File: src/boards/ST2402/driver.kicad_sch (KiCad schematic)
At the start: 49 parts, among them J15 Screw_Terminal_01x01, J16 Screw_Terminal_01x01, J17 Screw_Terminal_01x01, J9 Screw_Terminal_01x02, Q1 STB100N10F7, Q2 STB100N10F7, U1 L6494LD

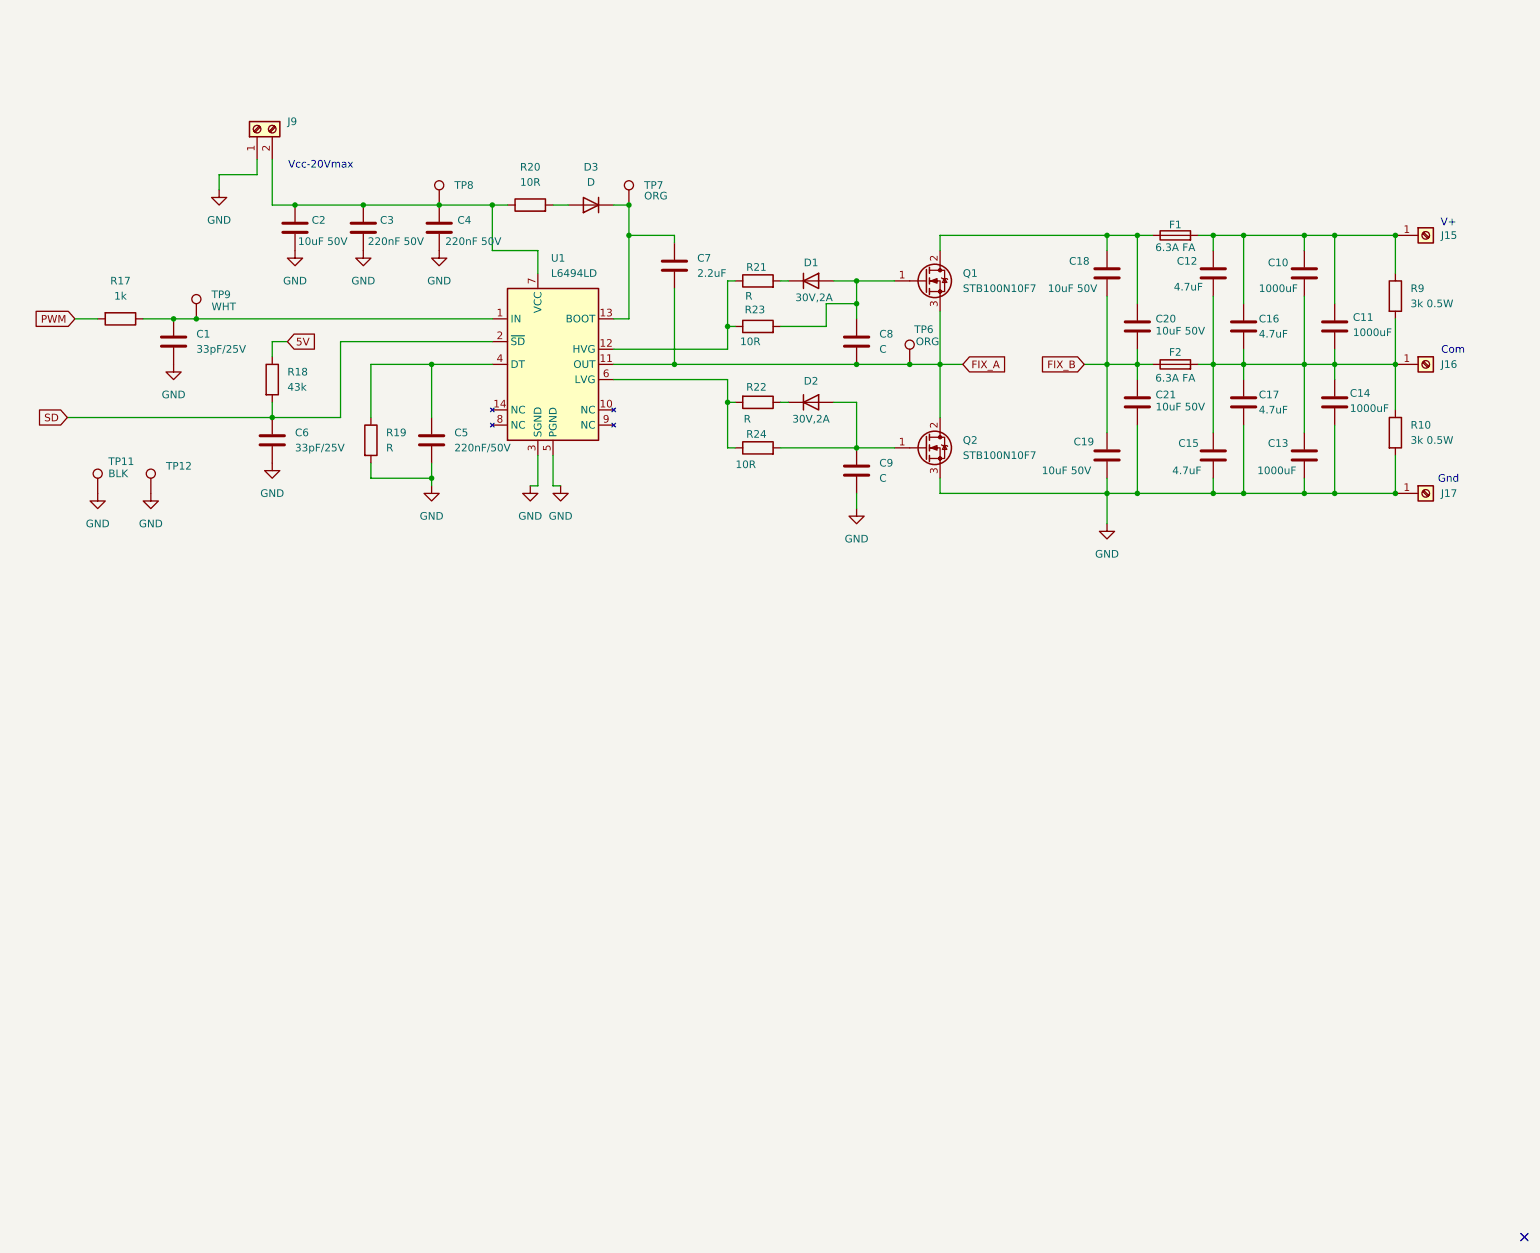
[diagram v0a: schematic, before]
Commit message: Updated pcb files
Added r2 and r3 gerbers and updated KiCad file (r3)
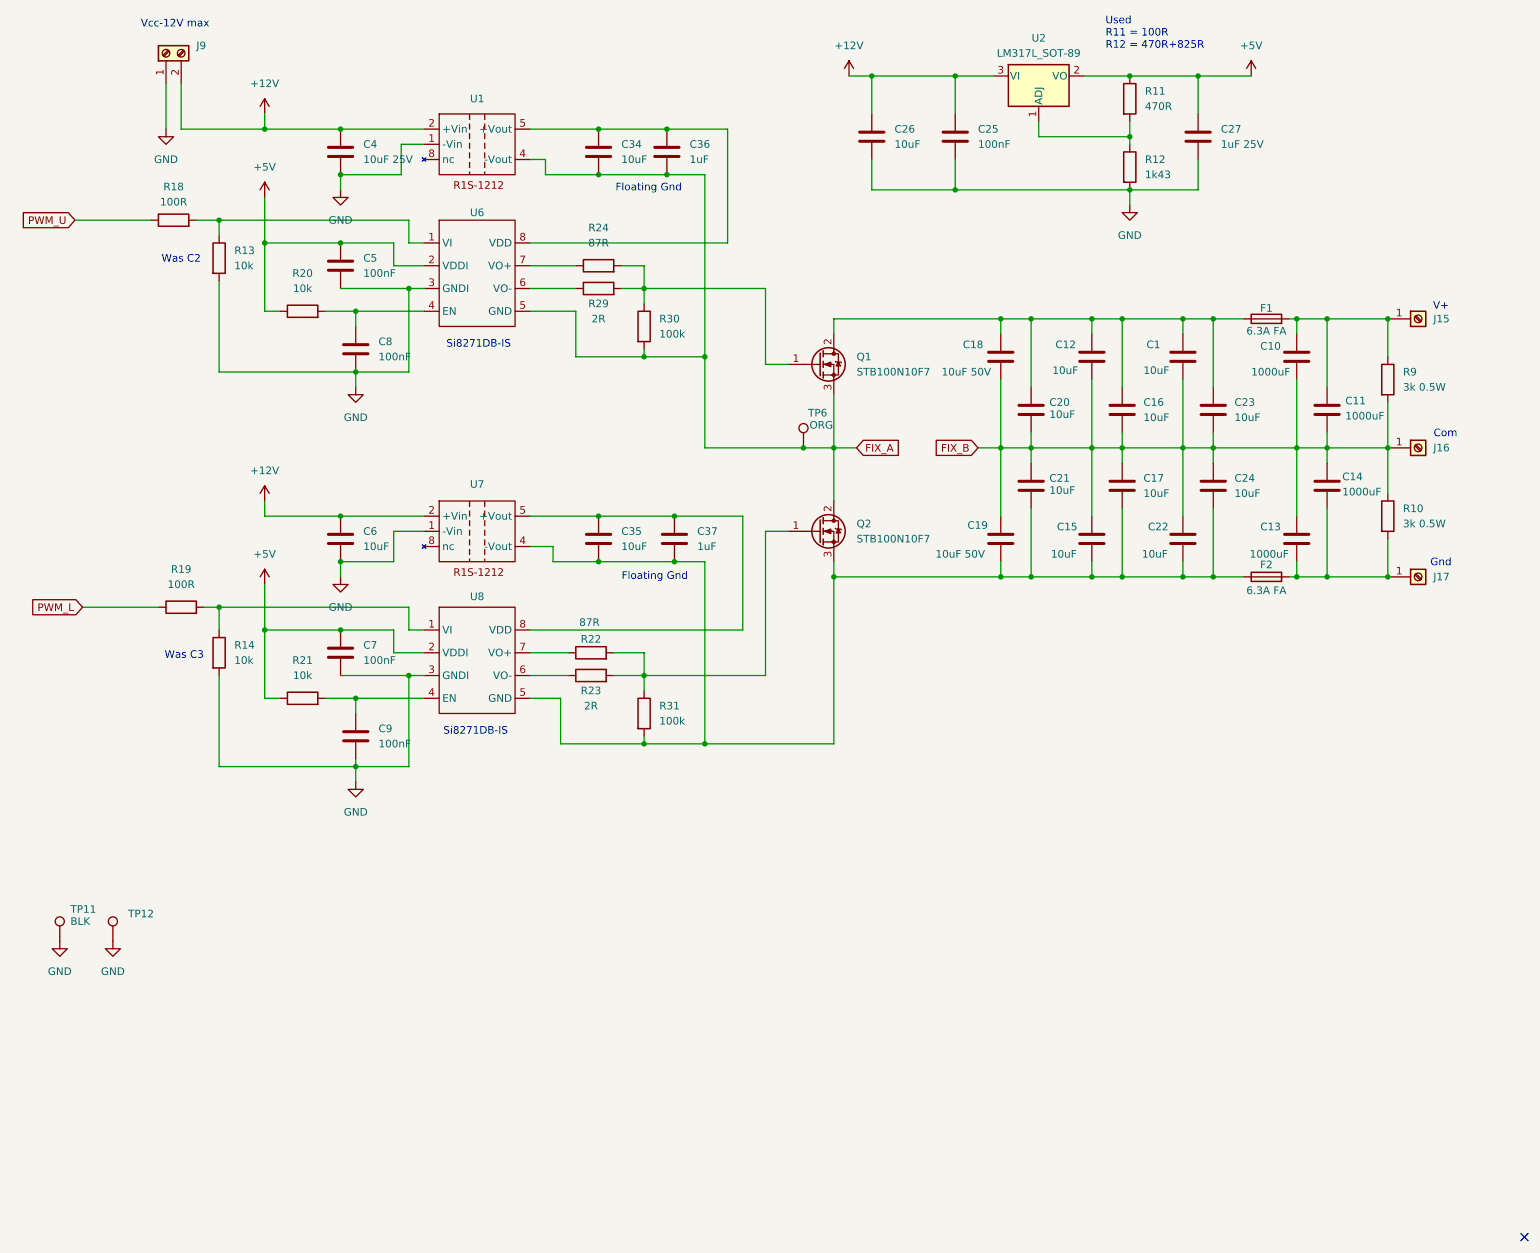
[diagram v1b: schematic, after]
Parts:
- removed C2: 10uF 50V, Capacitor_SMD:C_1206_3216Metric, symbol Device:C
- removed C3: 220nF 50V, Capacitor_SMD:C_0805_2012Metric, symbol Device:C
- removed D1, D2: 30V,2A, Diode_SMD:D_SMA, symbol Device:D
- removed D3: D, Diode_SMD:D_SMA, symbol Device:D
- removed R17: 1k, Resistor_SMD:R_0805_2012Metric, symbol Device:R
- removed TP7: ORG, TestPoint:TestPoint_THTPad_D2.0mm_Drill1.0mm, symbol Connector:TestPoint
- removed TP8: TestPoint, TestPoint:TestPoint_THTPad_D2.0mm_Drill1.0mm, symbol Connector:TestPoint
- removed TP9: WHT, TestPoint:TestPoint_THTPad_D2.0mm_Drill1.0mm, symbol Connector:TestPoint
- removed U1: L6494LD, Package_SO:SO-14_3.9x8.65mm_P1.27mm, symbol Driver_FET:L6491
- added C22, C23, C24: 10uF, Capacitor_SMD:C_1210_3225Metric, symbol Device:C
- added C25: 100nF, Capacitor_SMD:C_0805_2012Metric, symbol Device:C
- added C26, C34, C35: 10uF, Capacitor_SMD:C_0805_2012Metric, symbol Device:C
- added C27: 1uF 25V, Capacitor_SMD:C_0805_2012Metric, symbol Device:C
- added C36, C37: 1uF, Capacitor_SMD:C_0805_2012Metric, symbol Device:C
- added R11: 470R, Resistor_SMD:R_0805_2012Metric, symbol Device:R
- added R12: 1k43, Resistor_SMD:R_0805_2012Metric, symbol Device:R
- added R13, R14: 10k, Resistor_SMD:R_0805_2012Metric, symbol Device:R
- added R29: 2R, Resistor_SMD:R_0805_2012Metric, symbol Device:R
- added R30, R31: 100k, Resistor_SMD:R_0805_2012Metric, symbol Device:R
- added U1, U7: ~, GS_Library:5_pin_single_smd, symbol GS_Library:R1S-1212
- added U2: LM317L_SOT-89, Package_TO_SOT_SMD:SOT-89-3, symbol Regulator_Linear:LM317L_SOT-89
- added U6, U8: ~, Package_SO:SOIC-8_3.9x4.9mm_P1.27mm, symbol GS_Library:Si8271DB
- C1: value 33pF/25V -> 10uF; footprint Capacitor_SMD:C_0805_2012Metric -> Capacitor_SMD:C_1210_3225Metric
- C12, C15, C16, C17: value 4.7uF -> 10uF; footprint Capacitor_THT:C_Rect_L18.0mm_W11.0mm_P15.00mm_FKS3_FKP3 -> Capacitor_SMD:C_1210_3225Metric
- C20, C21: value 10uF 50V -> 10uF
- C4: value 220nF 50V -> 10uF 25V
- C5: value 220nF/50V -> 100nF
- C6: value 33pF/25V -> 10uF
- C7: value 2.2uF -> 100nF; footprint Capacitor_SMD:C_1206_3216Metric -> Capacitor_SMD:C_0805_2012Metric
- C8, C9: value C -> 100nF
- R18: value 43k -> 100R
- R19: value R -> 100R
- R20: value 10R -> 10k; footprint Resistor_SMD:R_1206_3216Metric -> Resistor_SMD:R_0805_2012Metric
- R21: value R -> 10k
- R22: value R -> 87R
- R23: value 10R -> 2R
- R24: value 10R -> 87R
- TP11, TP12, TP6: footprint TestPoint:TestPoint_THTPad_D2.0mm_Drill1.0mm -> TestPoint:TestPoint_Keystone_5010-5014_Multipurpose
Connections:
- net FIX_A: now also C34.2, C36.2, R30.2, U1.4 (-Vout), U6.5 (GND); no longer C7.2, C8.2
- net FIX_B: now also C1.2, C10.2, C11.2, C12.2, C13.1, C14.1, C15.1, C16.2, C17.1, J16.1 (Pin_1), R10.1, R9.2, C22.1, C23.2, C24.1; no longer F2.1
- net GND: now also C7.2, C8.2, C25.2, C26.2, C27.2, R12.2, R13.2, R14.2, U1.1 (-Vin), U6.3 (GNDI), U7.1 (-Vin), U8.3 (GNDI); no longer C1.2, C13.2, C14.2, C15.2, C17.2, C19.2, C21.2, J17.1 (Pin_1), Q2.3 (S), R10.2, R19.2
- net +12V: now reaches C4.1, J9.2 (Pin_2)
- net +12V: now also C6.1, C25.1, C26.1, U1.2 (+Vin), U2.3 (VI), U7.2 (+Vin); no longer R20.1
- net +5V: now reaches C5.1
- net +5V: now also C7.1, R20.1, R21.1, C27.1, R11.1, U2.2 (VO), U6.2 (VDDI), U8.2 (VDDI); no longer R19.1
- net at C10.1, C11.1, F1.2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: no longer C12.1, C16.1
- net at R23.1: now also U8.6 (VO-); no longer R21.1
- net at C1.1: now also C12.1, C16.1, C18.1, C20.1, F1.1, Q1.2 (D), C23.1
- net at R21.2: now also C9.1, U8.4 (EN)
- net at R20.2: now also C8.1, U6.4 (EN)
- net at R22.1: now also U8.7 (VO+)
- net at R22.2: now also Q2.1 (G), R23.2, R31.1; no longer R24.1
- net 5V renamed PWM_U
- net SD: no longer names the net of R18.2
- net SD: now also R13.1, U6.1 (VI); no longer C6.1
- new net: R14.1, R19.2, U8.1 (VI)
- new net: C15.2, C17.2, C19.2, C21.2, C22.2, C24.2, C35.2, C37.2, F2.1, Q2.3 (S), R31.2, U7.4 (-Vout), U8.5 (GND)
- new net: C35.1, C37.1, U7.5 (+Vout), U8.8 (VDD)
- new net: C13.2, C14.2, F2.2, J17.1 (Pin_1), R10.2
- new net: R24.1, U6.7 (VO+)
- new net: Q1.1 (G), R24.2, R29.2, R30.1
- new net: R11.2, R12.1, U2.1 (ADJ)
- new net: C34.1, C36.1, U1.5 (+Vout), U6.8 (VDD)
- new net: R29.1, U6.6 (VO-)
- new net PWM_L: R19.1
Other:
- note added: "Floating Gnd"
- note added: "Si8271DB-IS"
- note added: "Used R11 = 100R R12 = 470R+825R"
- note added: "Vcc-12V max"
- note added: "Was C2"
- note added: "Was C3"
- note removed: "Vcc-20Vmax"
- moved on the sheet: C10, C11, C12, C13, C14, C15, C16, C17, C18, C19, C20, C21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
